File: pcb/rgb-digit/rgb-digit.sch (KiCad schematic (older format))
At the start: 24 parts, among them J1 5V IN, J2 GND IN, J3 5V OUT, J4 GND OUT, J5 DATA IN, J6 DATA OUT, U1 WS2812B, U2 WS2812B, U3 WS2812B, U4 WS2812B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

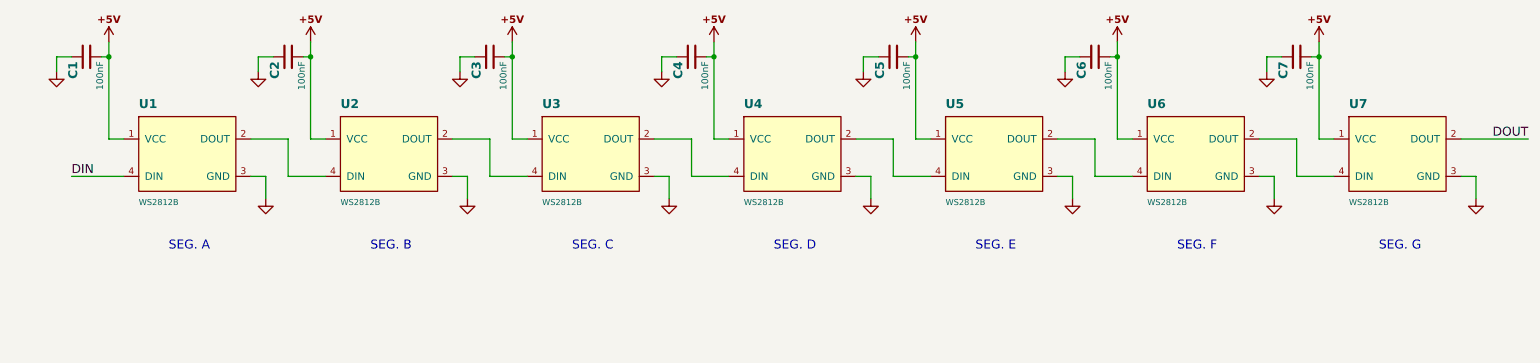
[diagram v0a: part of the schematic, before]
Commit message: Updated schematic of rgb-digits pcb * Changed sheet size to US letter * Added gerber and pdf files of each layers
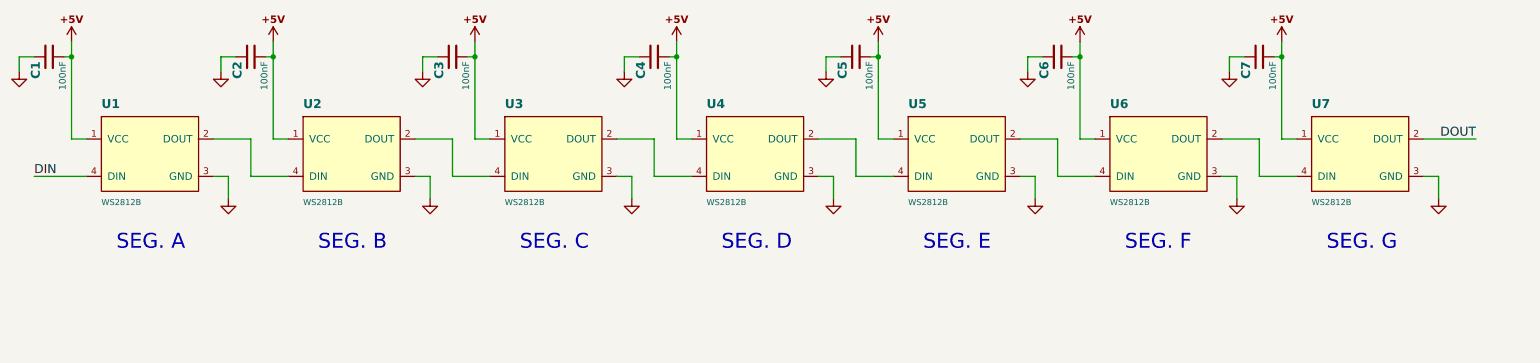
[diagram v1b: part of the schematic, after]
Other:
- moved on the sheet: C1, C2, C3, C4, C5, C6, C7, U1, U2, U3, U4, U5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

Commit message: Replaced RGB leds with IN-PI554FCH instead of WS2812B
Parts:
- C1, C2, C3, C4, C5, C6, C7: symbol CAP -> passive:CAP
- C8, C9: symbol CAP-E -> passive:CAP-E
- H1, H2: symbol Hole -> connectors:Hole
- J1, J2, J3, J4, J5, J6: symbol HEADER-1x01 -> connectors:HEADER-1x01
- U1, U2, U3, U4, U5, U6, U7: value WS2812B -> IN-PI554FCH; symbol WS2812B -> opto:WS2812B

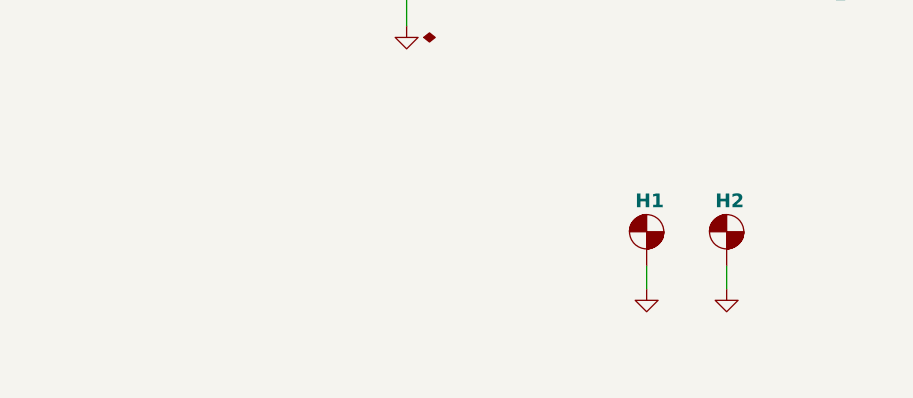
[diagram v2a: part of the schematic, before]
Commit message: Updated PCB design
+ Completed daughterboard PCB layout.
* Corrected soldermask clerance on front panel pcb.
- Removed input resistor on DIN for RGB lamp board.
* Modified PCB layout for PSU board.
* Updated gerber files.
* Updated schematics pdf, BOM.
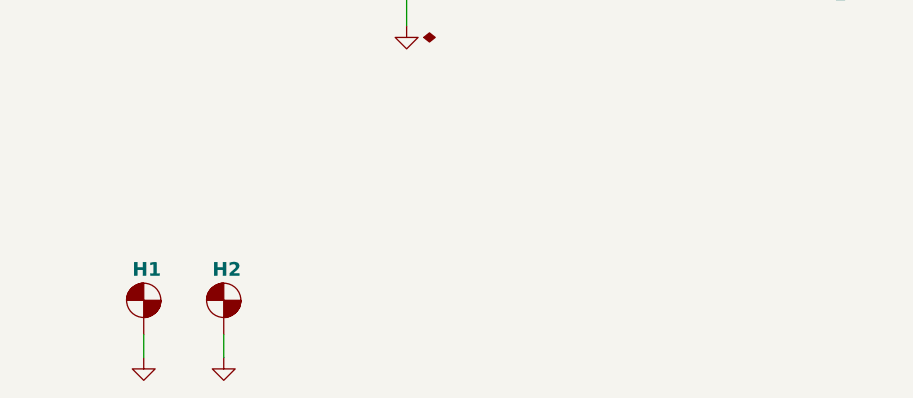
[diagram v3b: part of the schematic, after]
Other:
- moved on the sheet: H1, H2
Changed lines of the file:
@@
 L connectors:Hole H1
 U 1 1 56D81D00
-P 3400 6900
-F 0 "H1" H 3350 7000 60  0000 L BNB
-F 1 "Hole" H 3450 6800 40  0001 L TNN
-F 2 "Conn-Wire-Pads:Hole-Screw-#2" H 3450 6725 40  0001 L TNN
-F 3 "" H 3350 6975 60  0001 C CNN
-F 4 "Virtual" H 3350 7125 40  0001 L BNN "Family"
-	1    3400 6900
+P 1200 7200
+F 0 "H1" H 1150 7300 60  0000 L BNB
+F 1 "Hole" H 1250 7100 40  0001 L TNN
+F 2 "Conn-Wire-Pads:Hole-Screw-#2" H 1250 7025 40  0001 L TNN
+F 3 "" H 1150 7275 60  0001 C CNN
+F 4 "Virtual" H 1150 7425 40  0001 L BNN "Family"
+	1    1200 7200
 	1    0    0    -1
 $EndComp
@@
 L connectors:Hole H2
 U 1 1 56D81E39
-P 3750 6900
-F 0 "H2" H 3700 7000 60  0000 L BNB
-F 1 "Hole" H 3800 6800 40  0001 L TNN
-F 2 "Conn-Wire-Pads:Hole-Screw-#2" H 3800 6725 40  0001 L TNN
-F 3 "" H 3700 6975 60  0001 C CNN
-F 4 "Virtual" H 3700 7125 40  0001 L BNN "Family"
-	1    3750 6900
+P 1550 7200
+F 0 "H2" H 1500 7300 60  0000 L BNB
+F 1 "Hole" H 1600 7100 40  0001 L TNN
+F 2 "Conn-Wire-Pads:Hole-Screw-#2" H 1600 7025 40  0001 L TNN
+F 3 "" H 1500 7275 60  0001 C CNN
+F 4 "Virtual" H 1500 7425 40  0001 L BNN "Family"
+	1    1550 7200
 	1    0    0    -1
 $EndComp
@@
 L power:GND #PWR022
 U 1 1 56D81E88
-P 3400 7150
-F 0 "#PWR022" H 3400 7200 30  0001 C CNN
-F 1 "GND" H 3400 7025 30  0001 C CNN
-F 2 "" H 3400 7150 60  0000 C CNN
-F 3 "" H 3400 7150 60  0000 C CNN
-	1    3400 7150
+P 1200 7450
+F 0 "#PWR022" H 1200 7500 30  0001 C CNN
+F 1 "GND" H 1200 7325 30  0001 C CNN
+F 2 "" H 1200 7450 60  0000 C CNN
+F 3 "" H 1200 7450 60  0000 C CNN
+	1    1200 7450
 	1    0    0    -1
 $EndComp
@@
 L power:GND #PWR023
 U 1 1 56D81EC3
-P 3750 7150
-F 0 "#PWR023" H 3750 7200 30  0001 C CNN
-F 1 "GND" H 3750 7025 30  0001 C CNN
-F 2 "" H 3750 7150 60  0000 C CNN
-F 3 "" H 3750 7150 60  0000 C CNN
-	1    3750 7150
+P 1550 7450
+F 0 "#PWR023" H 1550 7500 30  0001 C CNN
+F 1 "GND" H 1550 7325 30  0001 C CNN
+F 2 "" H 1550 7450 60  0000 C CNN
+F 3 "" H 1550 7450 60  0000 C CNN
+	1    1550 7450
 	1    0    0    -1
 $EndComp
@@
 	10100 3100 10450 3100
 Wire Wire Line
-	3400 7050 3400 7150
-Wire Wire Line
-	3750 7050 3750 7150
+	1200 7350 1200 7450
+Wire Wire Line
+	1550 7350 1550 7450
 Wire Wire Line
 	1950 5150 2100 5150
